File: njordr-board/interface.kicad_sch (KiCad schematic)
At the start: 23 parts, among them IC101 DRV8300DPWR, J301 Conn_01x04, T3 TestPoint, T4 TestPoint, T5 TestPoint, T6 TestPoint, T7 TestPoint, T8 TestPoint, U1 ESDU5V0H4, U2 MT3608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

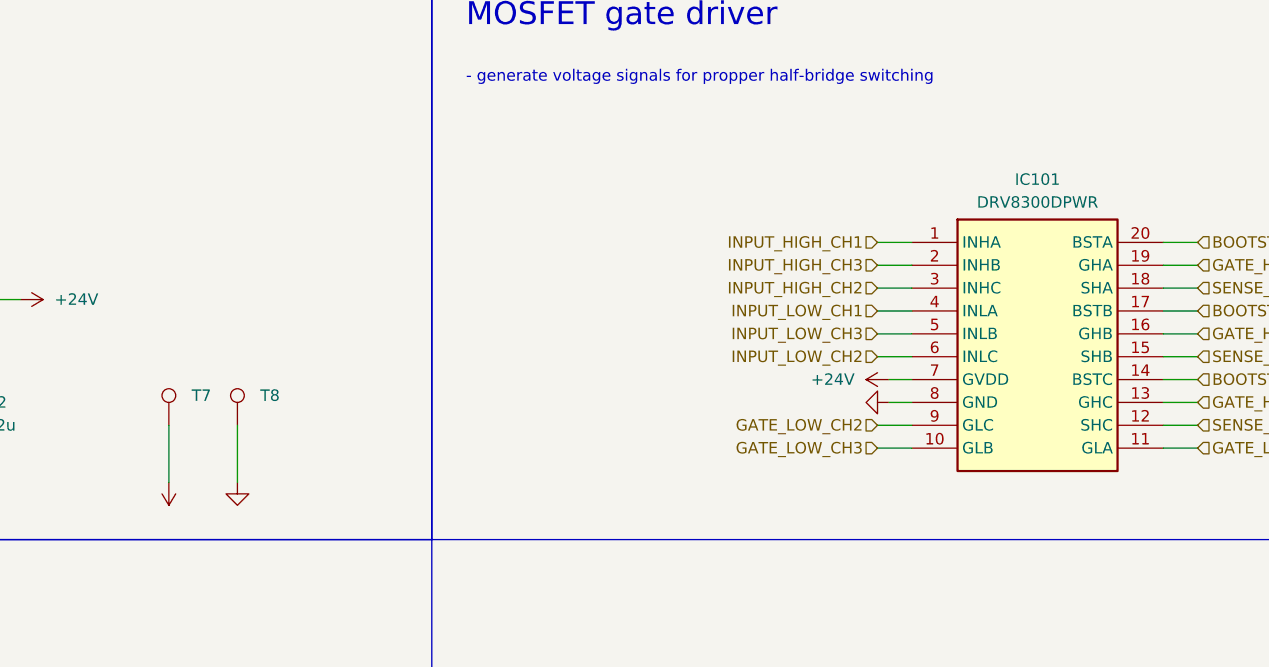
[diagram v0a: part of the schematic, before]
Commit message: board: Improve board markings
- rotate reference labels
- add connector description
- add logo
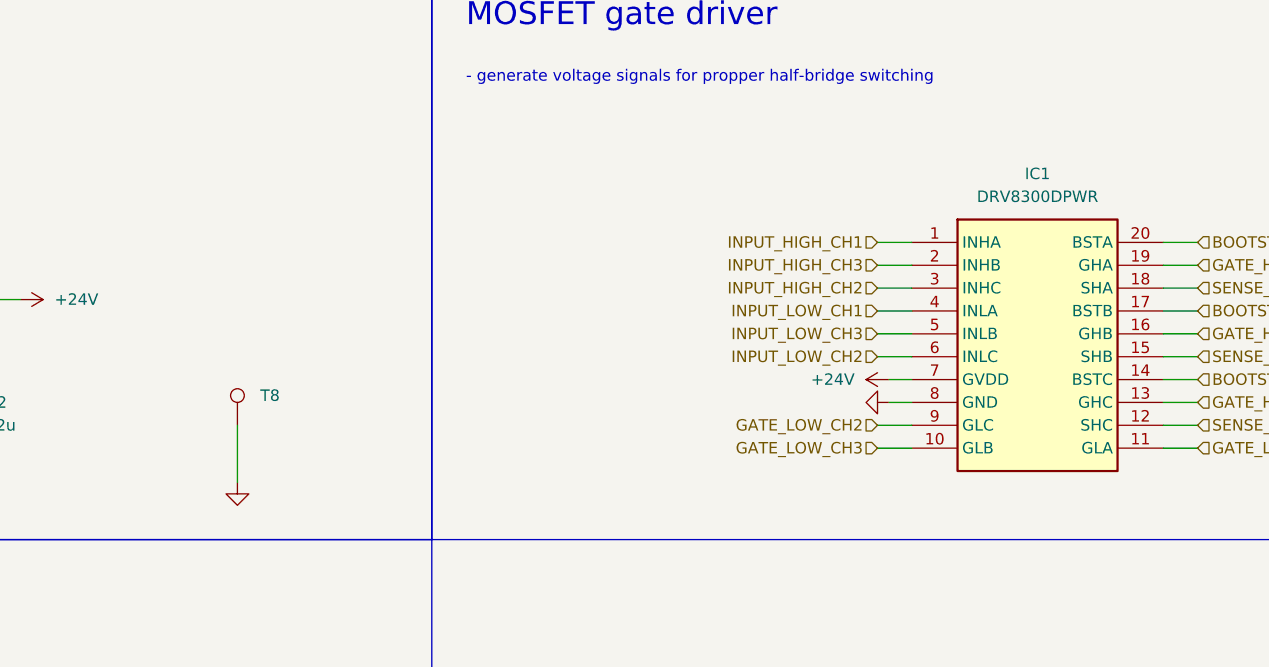
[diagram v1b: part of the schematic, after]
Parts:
- removed T7: TestPoint, TestPoint:TestPoint_Pad_1.0x1.0mm, symbol Connector:TestPoint
- T3, T6: Label (none) -> 3V3
- T4: Label (none) -> 24V
- T5: Label (none) -> 5V
- T8: Label (none) -> GND
- renumbered IC101 to IC1
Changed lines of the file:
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@@
 	(wire
 		(pts
-			(xy 119.38 76.2) (xy 119.38 82.55)
-		)
-		(stroke
-			(width 0)
-			(type default)
-		)
-	)
-	(wire
-		(pts
 			(xy 45.72 67.31) (xy 49.53 67.31)
 		)
@@
 			)
 		)
+		(property "Label" "GND"
+			(at 127 76.2 0)
+			(effects
+				(font
+					(size 1.27 1.27)
+				)
+				(hide yes)
+			)
+		)
 		(pin "1"
 		)
@@
 	)
 	(symbol
-		(lib_id "Connector:TestPoint")
-		(at 119.38 76.2 0)
-		(unit 1)
-		(exclude_from_sim yes)
-		(in_bom no)
-		(on_board no)
-		(dnp no)
-		(fields_autoplaced yes)
-		(property "Reference" "T7"
-			(at 121.92 72.8979 0)
-			(effects
-				(font
-					(size 1.27 1.27)
-				)
-				(justify left)
-			)
-		)
-		(property "Value" "TestPoint"
-			(at 121.92 74.1679 0)
-			(effects
-				(font
-					(size 1.27 1.27)
-				)
-				(justify left)
-				(hide yes)
-			)
-		)
-		(property "Footprint" "TestPoint:TestPoint_Pad_1.0x1.0mm"
-			(at 124.46 76.2 0)
-			(effects
-				(font
-					(size 1.27 1.27)
-				)
-				(hide yes)
-			)
-		)
-		(property "Datasheet" "~"
-			(at 124.46 76.2 0)
-			(effects
-				(font
-					(size 1.27 1.27)
-				)
-				(hide yes)
-			)
-		)
-		(property "Description" "test point"
-			(at 119.38 76.2 0)
-			(effects
-				(font
-					(size 1.27 1.27)
-				)
-				(hide yes)
-			)
-		)
-		(pin "1"
-		)
-		(instances
-			(project "njordr-board"
-				(path "/837a3018-1957-4824-b018-c0ef83e9cb67/085e2257-4ead-4630-86ba-fd69b8cd726d"
-					(reference "T7")
-					(unit 1)
-				)
-			)
-		)
-	)
-	(symbol
 		(lib_id "Device:L")
 		(at 68.58 52.07 90)
@@
 			)
 		)
+		(property "Label" "24V"
+			(at 95.25 53.34 0)
+			(effects
+				(font
+					(size 1.27 1.27)
+				)
+				(hide yes)
+			)
+		)
 		(pin "1"
 		)
@@
 			)
 		)
-		(pin "1"
-		)
-		(instances
-			(project "njordr-board"
-				(path "/837a3018-1957-4824-b018-c0ef83e9cb67/085e2257-4ead-4630-86ba-fd69b8cd726d"
-					(reference "T3")
-					(unit 1)
-				)
-			)
-		)
-	)
-	(symbol
-		(lib_id "power:+3.3V")
-		(at 119.38 82.55 180)
-		(unit 1)
-		(exclude_from_sim yes)
-		(in_bom no)
-		(on_board no)
-		(dnp no)
-		(fields_autoplaced yes)
-		(property "Reference" "#PWR054"
-			(at 119.38 78.74 0)
-			(effects
-				(font
-					(size 1.27 1.27)
-				)
-				(hide yes)
-			)
-		)
-		(property "Value" "+3.3V"
-			(at 119.38 87.63 0)
-			(effects
-				(font
-					(size 1.27 1.27)
-				)
-				(hide yes)
-			)
-		)
-		(property "Footprint" ""
-			(at 119.38 82.55 0)
-			(effects
-				(font
-					(size 1.27 1.27)
-				)
-				(hide yes)
-			)
-		)
-		(property "Datasheet" ""
-			(at 119.38 82.55 0)
-			(effects
-				(font
-					(size 1.27 1.27)
-				)
-				(hide yes)
-			)
-		)
-		(property "Description" "Power symbol creates a global label with name \"+3.3V\""
-			(at 119.38 82.55 0)
+		(property "Label" "3V3"
+			(at 49.53 63.5 0)
 			(effects
 				(font
@@
 			(project "njordr-board"
 				(path "/837a3018-1957-4824-b018-c0ef83e9cb67/085e2257-4ead-4630-86ba-fd69b8cd726d"
-					(reference "#PWR054")
+					(reference "T3")
 					(unit 1)
 				)
@@
 			)
 		)
+		(property "Label" "5V"
+			(at 288.29 237.49 0)
+			(effects
+				(font
+					(size 1.27 1.27)
+				)
+				(hide yes)
+			)
+		)
 		(pin "1"
 		)
@@
 			)
 		)
+		(property "Label" "3V3"
+			(at 311.15 237.49 0)
+			(effects
+				(font
+					(size 1.27 1.27)
+				)
+				(hide yes)
+			)
+		)
 		(pin "1"
 		)
@@
 		(dnp no)
 		(fields_autoplaced yes)
-		(property "Reference" "IC101"
-			(at 215.9 48.895 0)
+		(property "Reference" "IC1"
+			(at 215.9 48.26 0)
 			(effects
 				(font
@@
 		)
 		(property "Value" "DRV8300DPWR"
-			(at 215.9 51.435 0)
+			(at 215.9 50.8 0)
 			(effects
 				(font
@@
 			(project ""
 				(path "/837a3018-1957-4824-b018-c0ef83e9cb67/085e2257-4ead-4630-86ba-fd69b8cd726d"
-					(reference "IC101")
+					(reference "IC1")
 					(unit 1)
 				)

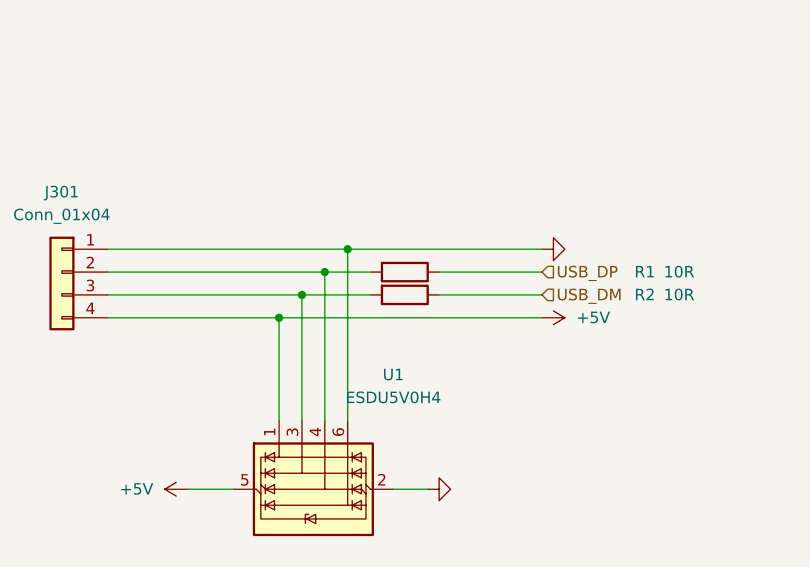
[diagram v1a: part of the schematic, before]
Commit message: njordr-board: Use updated library symbols and packages
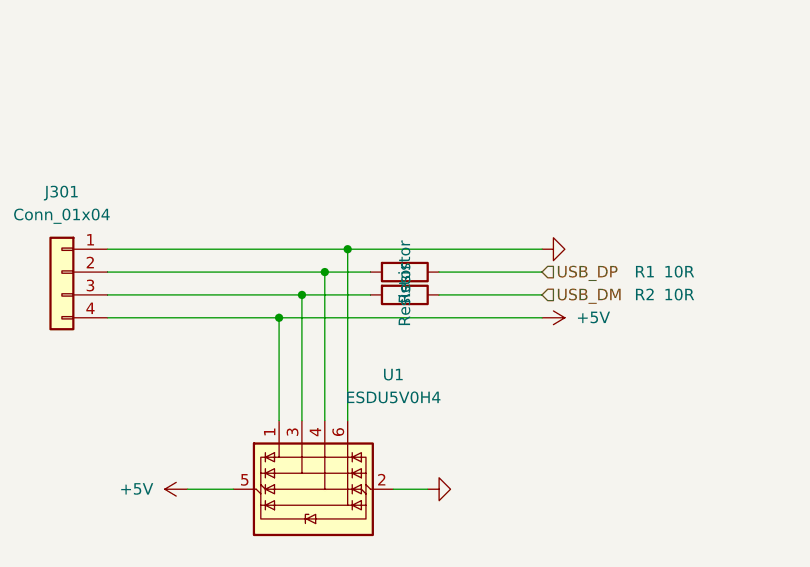
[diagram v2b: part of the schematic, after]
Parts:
- C1, C2, C3: footprint njordr:C_0805_2012Metric_Pad1.18x1.45mm_HandSolder -> njordr:C-0805-HandSolder
- C28, C29: footprint njordr:C_0603_1608Metric_Pad1.08x0.95mm_HandSolder -> njordr:C-0603-HandSolder
- D1: footprint njordr:D_SOD-323_HandSoldering -> njordr:D-SOD-323-HandSolder
- IC1: symbol DRV8300DPWR:DRV8300DPWR -> njordr:DRV8300DPWR; Arrow Part Number (none) -> DRV8300DPWR; Arrow Price/Stock (none) -> https://www.arrow.com/en/products/drv8300dpwr/texas-instrum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; Mouser Price/Stock (none) -> https://www.mouser.co.uk/ProductDetail/Texas-Instruments/DR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
- L1: footprint njordr:L_Axial_L7.0mm_D3.3mm_P10.16mm_Horizontal_Fastron_MICC -> njordr:L-Axial-L7.0-D3.3mm-P10.16
- R1, R2: footprint Capacitor_SMD:C_0603_1608Metric_Pad1.08x0.95mm_HandSolder -> njordr:C-0603-HandSolder
- R17, R18, R3: footprint njordr:R_0603_1608Metric_Pad0.98x0.95mm_HandSolder -> njordr:R-0603-HandSolder
- T3, T4: footprint njordr:TestPoint_Pad_1.0x1.0mm -> njordr:TestPoint-Pad-1.0x1.0
- U2: footprint njordr:SOT-23-6_Handsoldering -> njordr:SOT-23-6-HandSolder
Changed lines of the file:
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@@
 			)
 		)
-		(property "Footprint" "njordr:R_0603_1608Metric_Pad0.98x0.95mm_HandSolder"
+		(property "Footprint" "njordr:R-0603-HandSolder"
 			(at 55.118 57.15 90)
 			(effects
@@
 			)
 		)
-		(property "Datasheet" "https://jlcpcb.com/partdetail/26547-0603WAF1002T5E/C25804"
+		(property "Datasheet" "~"
 			(at 53.34 57.15 0)
 			(effects
@@
 	)
 	(symbol
-		(lib_name "GND_4")
 		(lib_id "power:GND")
 		(at 229.87 257.81 90)
@@
 			)
 		)
-		(property "Footprint" "njordr:C_0805_2012Metric_Pad1.18x1.45mm_HandSolder"
+		(property "Footprint" "njordr:C-0805-HandSolder"
 			(at 96.2152 78.74 0)
 			(effects
@@
 			)
 		)
-		(property "Datasheet" "https://jlcpcb.com/partdetail/46786-CL21A226MAQNNNE/C45783"
+		(property "Datasheet" "~"
 			(at 95.25 74.93 0)
 			(effects
@@
 			)
 		)
-		(property "Footprint" "njordr:R_0603_1608Metric_Pad0.98x0.95mm_HandSolder"
+		(property "Footprint" "njordr:R-0603-HandSolder"
 			(at 87.63 69.088 90)
 			(effects
@@
 			)
 		)
-		(property "Datasheet" "https://jlcpcb.com/partdetail/23864-0603WAF3303T5E/C23137"
+		(property "Datasheet" "~"
 			(at 87.63 67.31 0)
 			(effects
@@
 			)
 		)
-		(property "Footprint" "njordr:C_0603_1608Metric_Pad1.08x0.95mm_HandSolder"
+		(property "Footprint" "njordr:C-0603-HandSolder"
 			(at 77.1652 121.92 0)
 			(effects
@@
 			)
 		)
-		(property "Datasheet" "https://jlcpcb.com/api/file/downloadByFileSystemAccessId/8579707083955945472"
+		(property "Datasheet" "~"
 			(at 76.2 118.11 0)
 			(effects
@@
 			)
 		)
-		(property "Footprint" "Capacitor_SMD:C_0603_1608Metric_Pad1.08x0.95mm_HandSolder"
+		(property "Footprint" "njordr:C-0603-HandSolder"
 			(at 227.33 231.902 90)
 			(effects
@@
 			)
 		)
-		(property "Description" ""
+		(property "Description" "Resistor"
 			(at 227.33 233.68 0)
 			(effects
@@
 			)
 		)
-		(property "Footprint" "Capacitor_SMD:C_0603_1608Metric_Pad1.08x0.95mm_HandSolder"
+		(property "Footprint" "njordr:C-0603-HandSolder"
 			(at 227.33 234.442 90)
 			(effects
@@
 			)
 		)
-		(property "Description" ""
+		(property "Description" "Resistor"
 			(at 227.33 236.22 0)
 			(effects
@@
 			)
 		)
-		(property "Footprint" "njordr:L_Axial_L7.0mm_D3.3mm_P10.16mm_Horizontal_Fastron_MICC"
+		(property "Footprint" "njordr:L-Axial-L7.0-D3.3mm-P10.16"
 			(at 68.58 52.07 0)
 			(effects
@@
 			)
 		)
-		(property "Datasheet" "https://www.gme.cz/v/1484863/gym-cym-ec-24-6r8k-tb-tlumivka"
+		(property "Datasheet" "~"
 			(at 68.58 52.07 0)
 			(effects
@@
 			)
 		)
-		(property "Footprint" "njordr:C_0603_1608Metric_Pad1.08x0.95mm_HandSolder"
+		(property "Footprint" "njordr:C-0603-HandSolder"
 			(at 88.5952 121.92 0)
 			(effects
@@
 			)
 		)
-		(property "Datasheet" "https://jlcpcb.com/api/file/downloadByFileSystemAccessId/8579707083955945472"
+		(property "Datasheet" "~"
 			(at 87.63 118.11 0)
 			(effects
@@
 			)
 		)
-		(property "Footprint" "njordr:R_0603_1608Metric_Pad0.98x0.95mm_HandSolder"
+		(property "Footprint" "njordr:R-0603-HandSolder"
 			(at 81.788 74.93 90)
 			(effects
@@
 			)
 		)
-		(property "Datasheet" "https://jlcpcb.com/partdetail/26547-0603WAF1002T5E/C25804"
+		(property "Datasheet" "~"
 			(at 80.01 74.93 0)
 			(effects
@@
 			)
 		)
-		(property "Footprint" "njordr:TestPoint_Pad_1.0x1.0mm"
+		(property "Footprint" "njordr:TestPoint-Pad-1.0x1.0"
 			(at 100.33 53.34 0)
 			(effects
@@
 	)
 	(symbol
-		(lib_name "GND_4")
 		(lib_id "power:GND")
 		(at 242.57 231.14 90)
@@
 			)
 		)
-		(property "Datasheet" "https://jlcpcb.com/partdetail/Advanced_MonolithicSystems-AMS1117_33/C6186"
+		(property "Datasheet" "http://www.advanced-monolithic.com/pdf/ds1117.pdf"
 			(at 302.26 247.65 0)
 			(effects
@@
 			)
 		)
-		(property "Footprint" "njordr:SOT-23-6_Handsoldering"
+		(property "Footprint" "njordr:SOT-23-6-HandSolder"
 			(at 69.85 71.12 0)
 			(effects
@@
 			)
 		)
-		(property "Datasheet" "https://jlcpcb.com/partdetail/XI_AN_AerosemiTech-MT3608/C84817"
+		(property "Datasheet" "https://www.olimex.com/Products/Breadboarding/BB-PWR-3608/resources/MT3608.pdf"
 			(at 62.23 53.34 0)
 			(effects
@@
 			)
 		)
-		(property "Footprint" "njordr:D_SOD-323_HandSoldering"
+		(property "Footprint" "njordr:D-SOD-323-HandSolder"
 			(at 87.63 57.785 0)
 			(effects
@@
 			)
 		)
-		(property "Datasheet" "https://jlcpcb.com/partdetail/GuangdongHottech-1N5819WS/C191023"
+		(property "Datasheet" "https://datasheet.lcsc.com/lcsc/2204281430_Guangdong-Hottech-1N5819WS_C191023.pdf"
 			(at 87.63 62.23 0)
 			(effects
@@
 			)
 		)
-		(property "Footprint" "njordr:TestPoint_Pad_1.0x1.0mm"
+		(property "Footprint" "njordr:TestPoint-Pad-1.0x1.0"
 			(at 54.61 63.5 0)
 			(effects
@@
 			)
 		)
-		(property "Footprint" "njordr:C_0805_2012Metric_Pad1.18x1.45mm_HandSolder"
+		(property "Footprint" "njordr:C-0805-HandSolder"
 			(at 312.1152 252.73 0)
 			(effects
@@
 			)
 		)
-		(property "Datasheet" "https://jlcpcb.com/partdetail/46786-CL21A226MAQNNNE/C45783"
+		(property "Datasheet" "~"
 			(at 311.15 248.92 0)
 			(effects
@@
 			)
 		)
-		(property "Footprint" "njordr:C_0805_2012Metric_Pad1.18x1.45mm_HandSolder"
+		(property "Footprint" "njordr:C-0805-HandSolder"
 			(at 58.1152 78.74 0)
 			(effects
@@
 			)
 		)
-		(property "Datasheet" "https://jlcpcb.com/partdetail/46786-CL21A226MAQNNNE/C45783"
+		(property "Datasheet" "~"
 			(at 57.15 74.93 0)
 			(effects
@@
 	)
 	(symbol
-		(lib_id "DRV8300DPWR:DRV8300DPWR")
+		(lib_id "njordr:DRV8300DPWR")
 		(at 201.93 55.88 0)
 		(unit 1)
-		(exclude_from_sim yes)
+		(exclude_from_sim no)
 		(in_bom yes)
 		(on_board yes)
@@
 				(hide yes)
 			)
+		)
+		(property "Mouser Price/Stock" "https://www.mouser.co.uk/ProductDetail/Texas-Instruments/DRV8300DPWR?qs=eP2BKZSCXI6qJbKdYnGwBg%3D%3D"
+			(at 226.06 850.8 0)
+			(effects
+				(font
+					(size 1.27 1.27)
+				)
+				(justify left top)
+				(hide yes)
+			)
+		)
+		(property "Arrow Part Number" "DRV8300DPWR"
+			(at 226.06 950.8 0)
+			(effects
+				(font
+					(size 1.27 1.27)
+				)
+				(justify left top)
+				(hide yes)
+			)
+		)
+		(property "Arrow Price/Stock" "https://www.arrow.com/en/products/drv8300dpwr/texas-instruments?utm_currency=USD&region=nac"
+			(at 226.06 1050.8 0)
+			(effects
+				(font
+					(size 1.27 1.27)
+				)
+				(justify left top)
+				(hide yes)
+			)
